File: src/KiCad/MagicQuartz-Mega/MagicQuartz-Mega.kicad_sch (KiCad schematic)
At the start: 33 parts, among them J1 Analog Out, J2 Power, J3 DC/DC, J4 Sensor, SW1 Left, SW2 Right, SW3 Down, SW4 Up, U1 MEGA_2560_PRO, U2 LM358

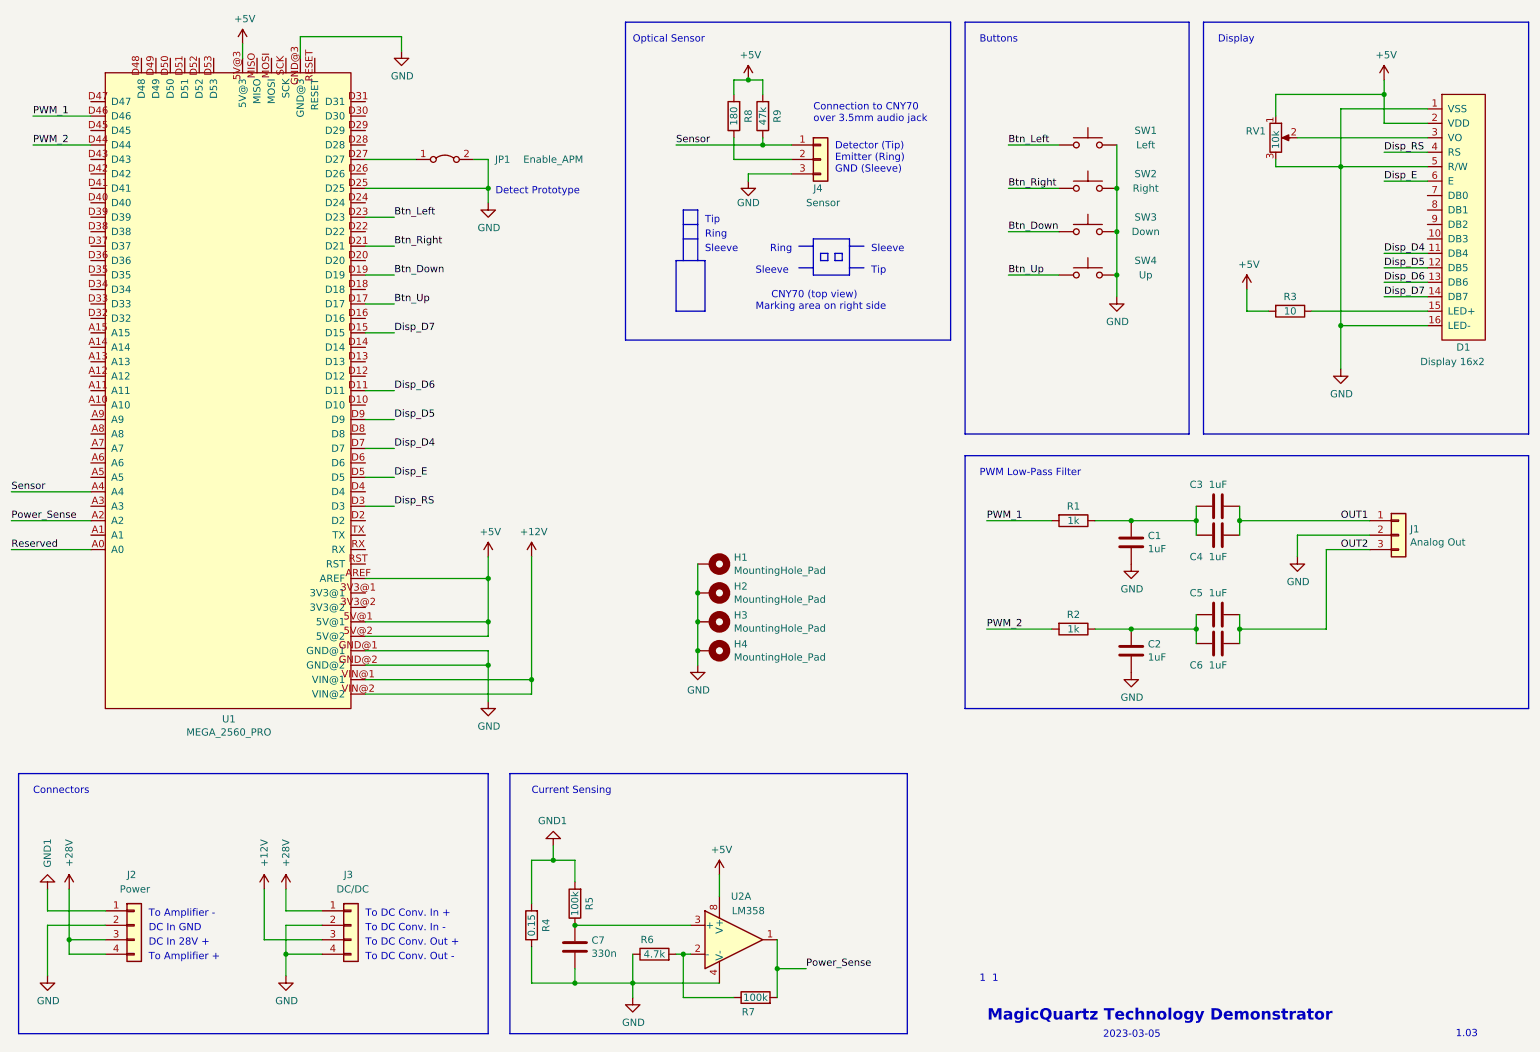
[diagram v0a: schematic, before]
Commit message: Update to 1.04
Clarify voltages and update documentation
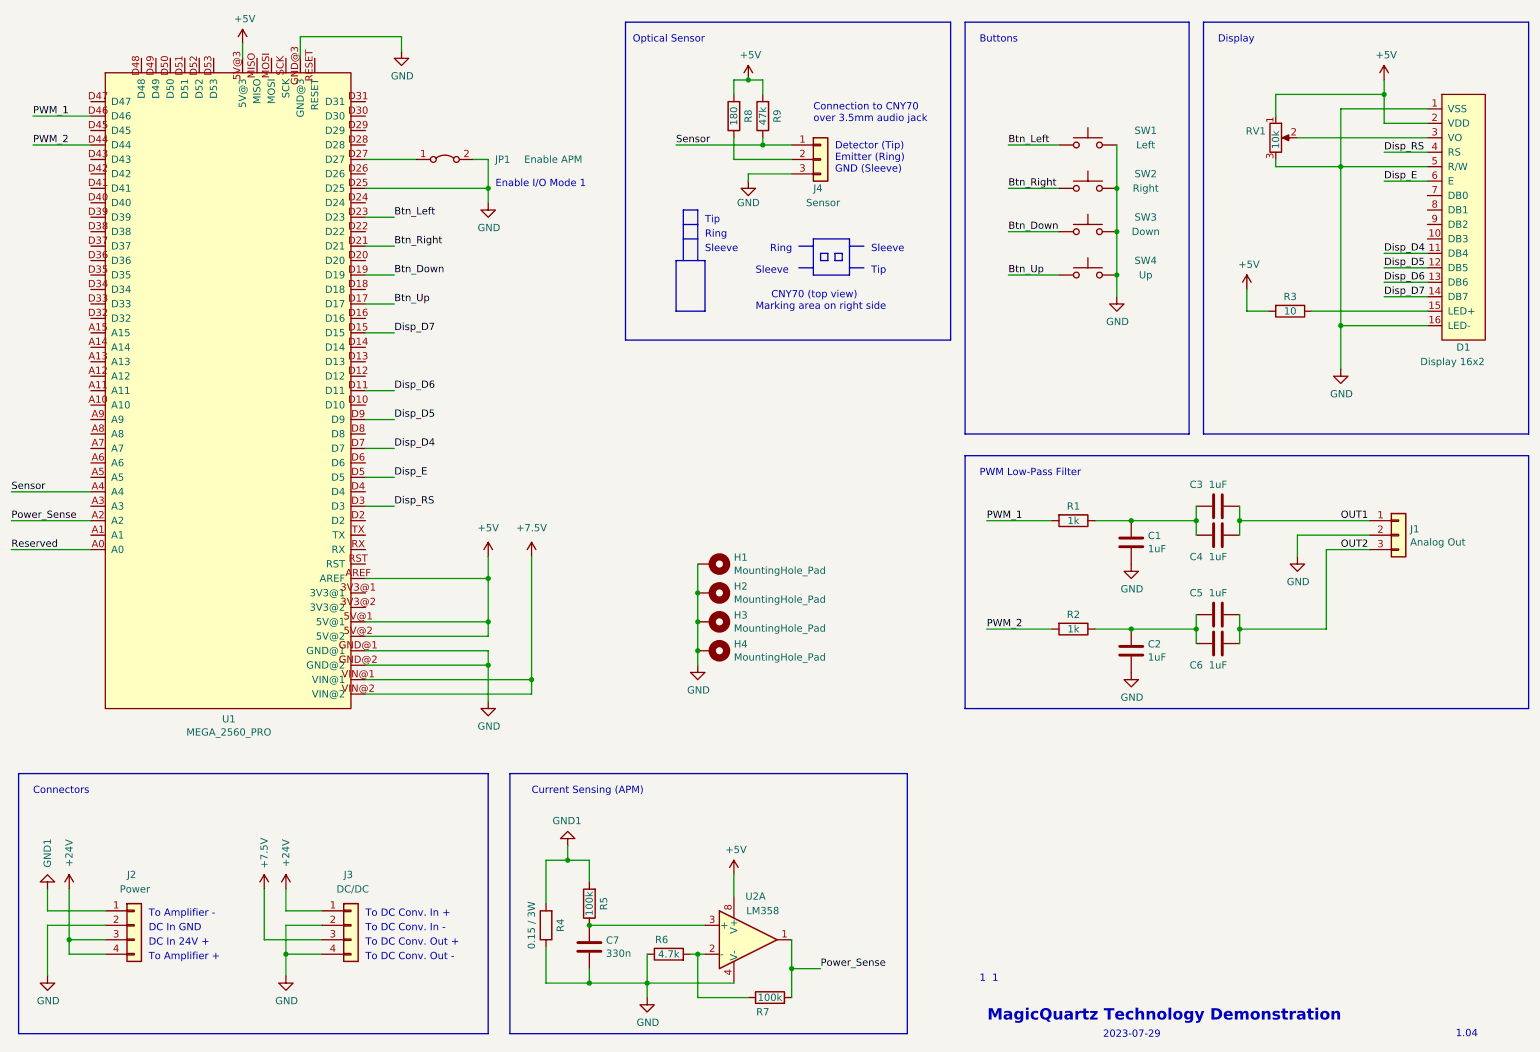
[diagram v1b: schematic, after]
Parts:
- JP1: value Enable_APM -> Enable APM
- R4: value 0.15 -> 0.15 / 3W
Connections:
- net +12V renamed +7.5V
- net +28V renamed +24V
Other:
- note added: "1.04"
- note added: "2023-07-29"
- note added: "Current Sensing (APM)"
- note added: "DC In 24V +"
- note added: "Enable I/O Mode 1"
- note added: "MagicQuartz Technology Demonstration"
- note removed: "1.03"
- note removed: "2023-03-05"
- note removed: "Current Sensing"
- note removed: "DC In 28V +"
- note removed: "Detect Prototype"
- note removed: "MagicQuartz Technology Demonstrator"
- moved on the sheet: C7, R4, R5, R6, R7, U2A
